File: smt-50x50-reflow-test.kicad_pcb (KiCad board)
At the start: 4 copper layers, 50 x 50 mm, 96 parts, among them J1 Conn_01x04_Pin, J2 Conn_01x02, J4 USB_C_Receptacle_USB2.0_14P, J8 Conn_01x04_Pin, J9 Conn_01x03_Pin, SW1 SW_Push, SW2 SW_Push, U1 ESP32-C6, U14 TMP117AIDRV, U15 BMP581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

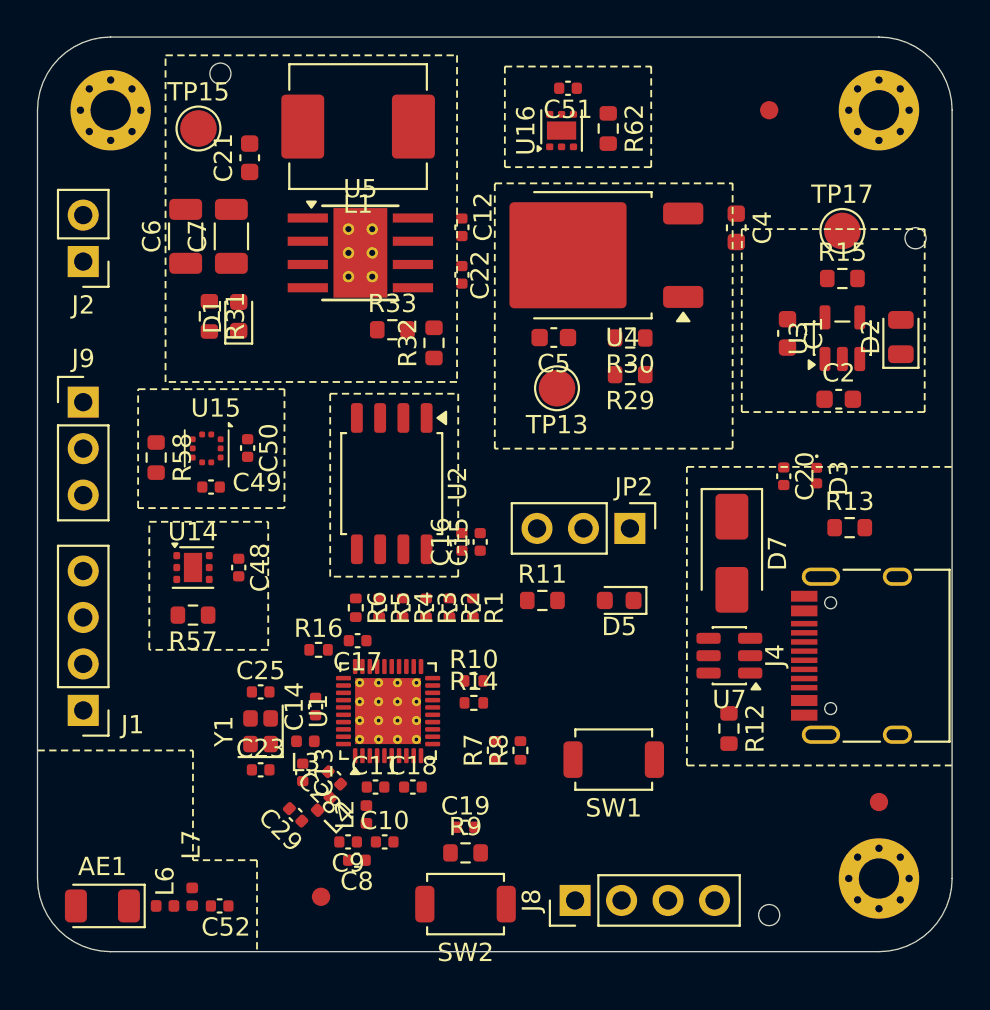
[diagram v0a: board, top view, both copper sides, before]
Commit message: pcb: align headers on a 2.54mm grid
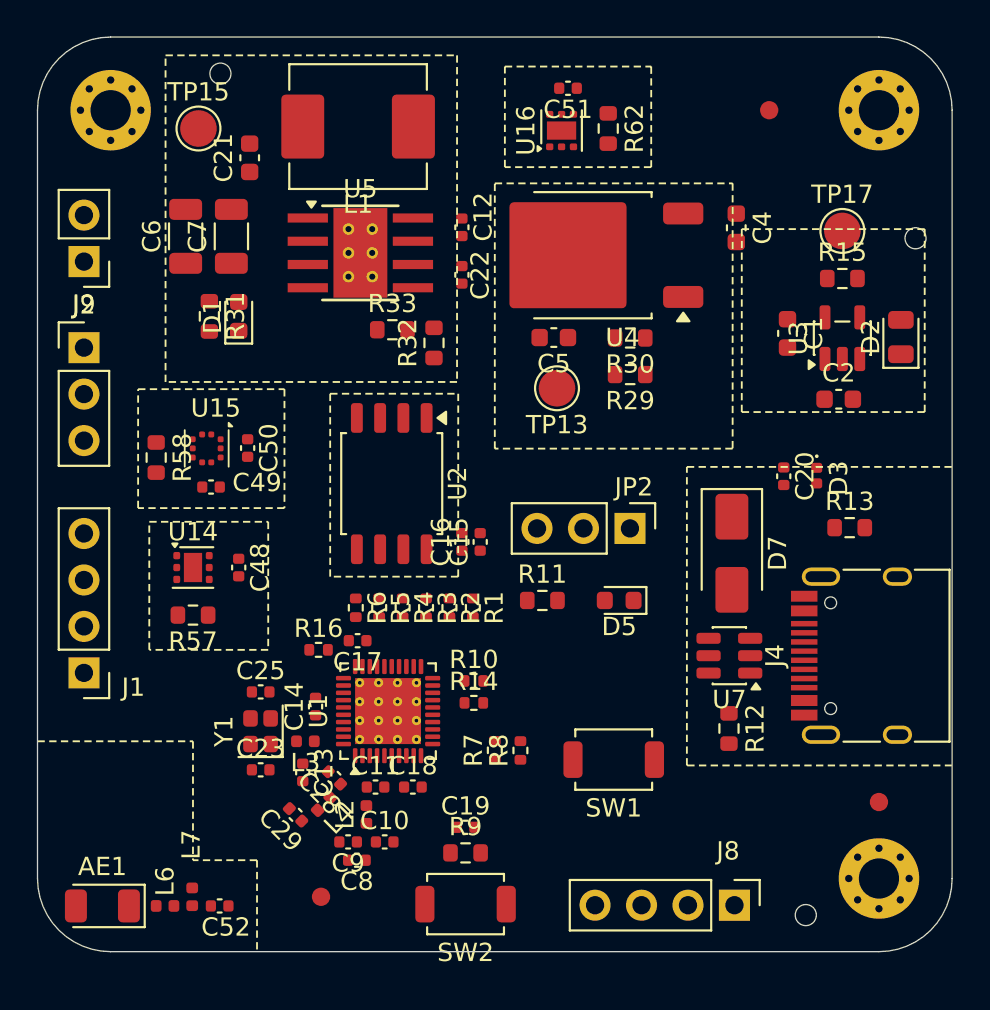
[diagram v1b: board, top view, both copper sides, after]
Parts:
- moved J8 8.71 mm to (173.1, 122.5), turned to -90 degrees
- moved J9 2.98 mm to (137.5, 92.0)
- moved J1 2.05 mm to (137.5, 109.8)
- moved REF** 2.00 mm to (177.0, 123.0)
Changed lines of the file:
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@@
 	(footprint "Connector_PinHeader_2.54mm:PinHeader_1x02_P2.54mm_Vertical"
 		(layer "F.Cu")
-		(at 137.5 87.275 180)
+		(at 137.54 87.275 180)
 		(descr "Through hole straight pin header, 1x02, 2.54mm pitch, single row")
 		(tags "Through hole pin header THT 1x02 2.54mm single row")
@@
 	(footprint "MountingHole:ToolingHole_1.152mm"
 		(layer "F.Cu")
-		(at 175 123)
+		(at 177 123)
 		(descr "Tooling Hole 1.152mm, 1.3mm solder mask, JLCPCB specification, https://jlcpcb.com/help/article/How-to-add-tooling-holes-for-PCB-assembly-order")
 		(tags "mounting")
@@
 			(polygon
 				(pts
-					(xy 175.7 123) (xy 175.679659 122.832479) (xy 175.619819 122.674694) (xy 175.523958 122.535814)
-					(xy 175.397645 122.423911) (xy 175.248223 122.345489) (xy 175.084376 122.305104) (xy 174.915624 122.305104)
-					(xy 174.751777 122.345489) (xy 174.602355 122.423911) (xy 174.476042 122.535814) (xy 174.380181 122.674694)
-					(xy 174.320341 122.832479) (xy 174.3 123) (xy 174.320341 123.167521) (xy 174.380181 123.325306)
-					(xy 174.476042 123.464186) (xy 174.602355 123.576089) (xy 174.751777 123.654511) (xy 174.915624 123.694896)
-					(xy 175.084376 123.694896) (xy 175.248223 123.654511) (xy 175.397645 123.576089) (xy 175.523958 123.464186)
-					(xy 175.619819 123.325306) (xy 175.679659 123.167521)
+					(xy 177.7 123) (xy 177.679659 122.832479) (xy 177.619819 122.674694) (xy 177.523958 122.535814)
+					(xy 177.397645 122.423911) (xy 177.248223 122.345489) (xy 177.084376 122.305104) (xy 176.915624 122.305104)
+					(xy 176.751777 122.345489) (xy 176.602355 122.423911) (xy 176.476042 122.535814) (xy 176.380181 122.674694)
+					(xy 176.320341 122.832479) (xy 176.3 123) (xy 176.320341 123.167521) (xy 176.380181 123.325306)
+					(xy 176.476042 123.464186) (xy 176.602355 123.576089) (xy 176.751777 123.654511) (xy 176.915624 123.694896)
+					(xy 177.084376 123.694896) (xy 177.248223 123.654511) (xy 177.397645 123.576089) (xy 177.523958 123.464186)
+					(xy 177.619819 123.325306) (xy 177.679659 123.167521)
 				)
 			)
@@
 	(footprint "Connector_PinHeader_2.54mm:PinHeader_1x04_P2.54mm_Vertical"
 		(layer "F.Cu")
-		(at 164.39 122.2 90)
+		(at 173.1 122.46 -90)
 		(descr "Through hole straight pin header, 1x04, 2.54mm pitch, single row")
 		(tags "Through hole pin header THT 1x04 2.54mm single row")
 		(property "Reference" "J8"
-			(at 0 -2.38 90)
+			(at -2.96 0.35 180)
 			(layer "F.SilkS")
 			(effects
@@
 		(attr through_hole exclude_from_bom)
 		(fp_line
-			(start -1.38 -1.38)
-			(end 0 -1.38)
+			(start -1.38 9)
+			(end 1.38 9)
 			(stroke
 				(width 0.12)
@@
 		)
 		(fp_line
-			(start -1.38 0)
-			(end -1.38 -1.38)
+			(start -1.38 1.27)
+			(end -1.38 9)
 			(stroke
 				(width 0.12)
@@
 		)
 		(fp_line
-			(start 1.38 1.27)
-			(end 1.38 9)
+			(start -1.38 1.27)
+			(end 1.38 1.27)
 			(stroke
 				(width 0.12)
@@
 		)
 		(fp_line
-			(start -1.38 1.27)
-			(end 1.38 1.27)
+			(start 1.38 1.27)
+			(end 1.38 9)
 			(stroke
 				(width 0.12)
@@
 		)
 		(fp_line
-			(start -1.38 1.27)
-			(end -1.38 9)
+			(start -1.38 0)
+			(end -1.38 -1.38)
 			(stroke
 				(width 0.12)
@@
 		)
 		(fp_line
-			(start -1.38 9)
-			(end 1.38 9)
+			(start -1.38 -1.38)
+			(end 0 -1.38)
 			(stroke
 				(width 0.12)
@@
 		)
 		(fp_line
-			(start 1.77 -1.77)
-			(end -1.77 -1.77)
+			(start -1.77 9.39)
+			(end 1.77 9.39)
 			(stroke
 				(width 0.05)
@@
 		)
 		(fp_line
-			(start -1.77 -1.77)
-			(end -1.77 9.39)
+			(start 1.77 9.39)
+			(end 1.77 -1.77)
 			(stroke
 				(width 0.05)
@@
 		)
 		(fp_line
-			(start 1.77 9.39)
-			(end 1.77 -1.77)
+			(start -1.77 -1.77)
+			(end -1.77 9.39)
 			(stroke
 				(width 0.05)
@@
 		)
 		(fp_line
-			(start -1.77 9.39)
-			(end 1.77 9.39)
+			(start 1.77 -1.77)
+			(end -1.77 -1.77)
 			(stroke
 				(width 0.05)
@@
 		)
 		(fp_line
-			(start 1.27 -1.27)
-			(end 1.27 8.89)
+			(start -1.27 8.89)
+			(end -1.27 -0.635)
 			(stroke
 				(width 0.1)
@@
 		)
 		(fp_line
-			(start -0.635 -1.27)
-			(end 1.27 -1.27)
+			(start 1.27 8.89)
+			(end -1.27 8.89)
 			(stroke
 				(width 0.1)
@@
 		)
 		(fp_line
-			(start 1.27 8.89)
-			(end -1.27 8.89)
+			(start -0.635 -1.27)
+			(end 1.27 -1.27)
 			(stroke
 				(width 0.1)
@@
 		)
 		(fp_line
-			(start -1.27 8.89)
-			(end -1.27 -0.635)
+			(start 1.27 -1.27)
+			(end 1.27 8.89)
 			(stroke
 				(width 0.1)
@@
 		)
 		(pad "1" thru_hole rect
-			(at 0 0 90)
+			(at 0 0 270)
 			(size 1.7 1.7)
 			(drill 1)
@@
 		)
 		(pad "2" thru_hole circle
-			(at 0 2.54 90)
+			(at 0 2.54 270)
 			(size 1.7 1.7)
 			(drill 1)
@@
 		)
 		(pad "3" thru_hole circle
-			(at 0 5.08 90)
+			(at 0 5.08 270)
 			(size 1.7 1.7)
 			(drill 1)
@@
 		)
 		(pad "4" thru_hole circle
-			(at 0 7.62 90)
+			(at 0 7.62 270)
 			(size 1.7 1.7)
 			(drill 1)
@@
 	(footprint "Connector_PinHeader_2.54mm:PinHeader_1x04_P2.54mm_Vertical"
 		(layer "F.Cu")
-		(at 137.5 111.81 180)
+		(at 137.54 109.76 180)
 		(descr "Through hole straight pin header, 1x04, 2.54mm pitch, single row")
 		(tags "Through hole pin header THT 1x04 2.54mm single row")
@@
 	(footprint "Connector_PinHeader_2.54mm:PinHeader_1x03_P2.54mm_Vertical"
 		(layer "F.Cu")
-		(at 137.5 94.96)
+		(at 137.54 91.98)
 		(descr "Through hole straight pin header, 1x03, 2.54mm pitch, single row")
 		(tags "Through hole pin header THT 1x03 2.54mm single row")
@@
 	)
 	(gr_line
-		(start 135 114)
-		(end 143.5 114)
+		(start 135 113.5)
+		(end 143.5 113.5)
 		(stroke
 			(width 0.1)
@@
 	)
 	(gr_line
-		(start 143.5 114)
+		(start 143.5 113.5)
 		(end 143.5 120)
 		(stroke

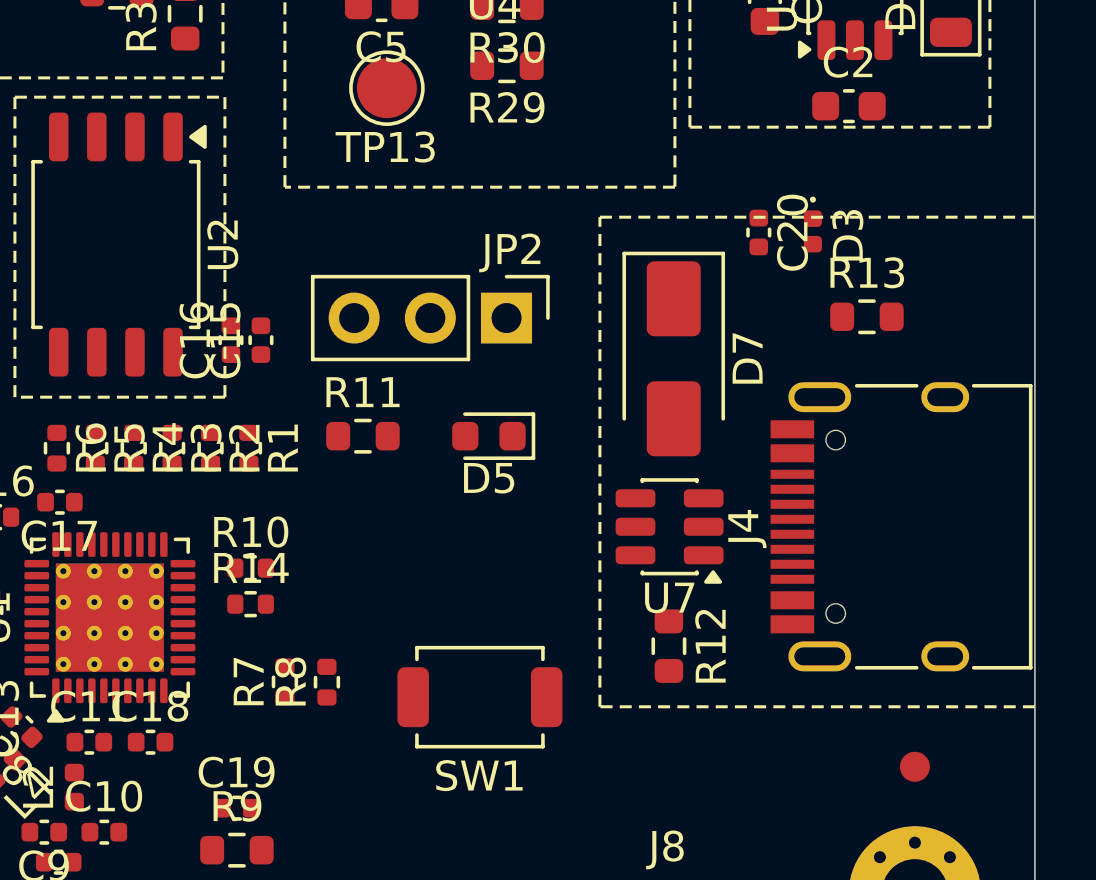
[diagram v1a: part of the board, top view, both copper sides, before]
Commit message: pcb: add usb routing
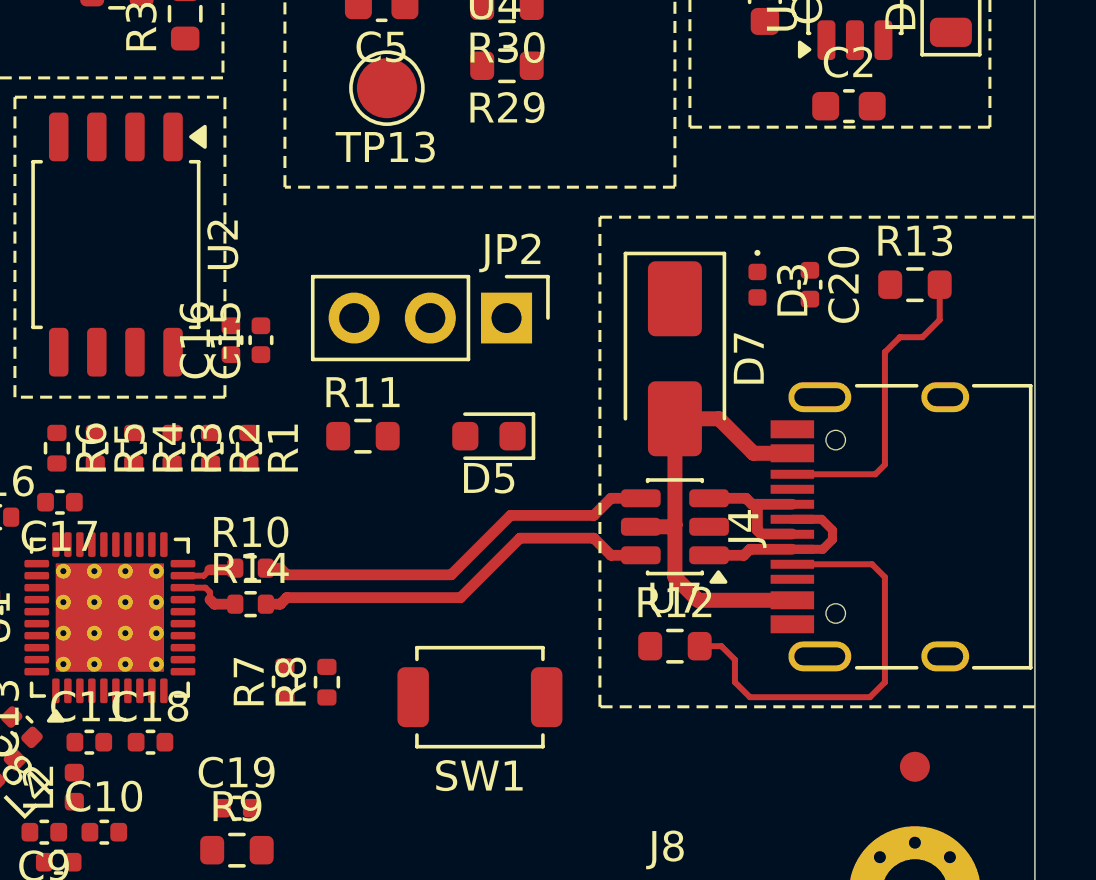
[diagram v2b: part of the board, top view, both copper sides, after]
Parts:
- moved D3 2.61 mm to (175.8, 100.8)
- moved C20 2.44 mm to (177.5, 100.8)
- moved R13 1.92 mm to (181.0, 100.8)
- moved R12 0.20 mm to (173.0, 112.8), turned to 0 degrees
- moved U7 0.18 mm to (173.0, 108.8)
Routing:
- net VBUS: track 0.00 -> 15.1 mm
- net Net-(J4-CC1): track 0.00 -> 14.3 mm
- net /D+: track 0.00 -> 13.6 mm
- net /D-: track 0.00 -> 13.6 mm
- net Net-(J4-CC2): track 0.00 -> 10.4 mm
- net Net-(J4-D--PadA7): track 0.00 -> 6.13 mm
- net Net-(J4-D+-PadA6): track 0.00 -> 4.95 mm
- net /ESP_D-: track 0.00 -> 2.12 mm
- net /ESP_D+: track 0.00 -> 1.85 mm

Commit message: pcb: add internal gnd planes
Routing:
- added copper zone on In1.Cu, net GND
- added copper zone on In2.Cu, net GND

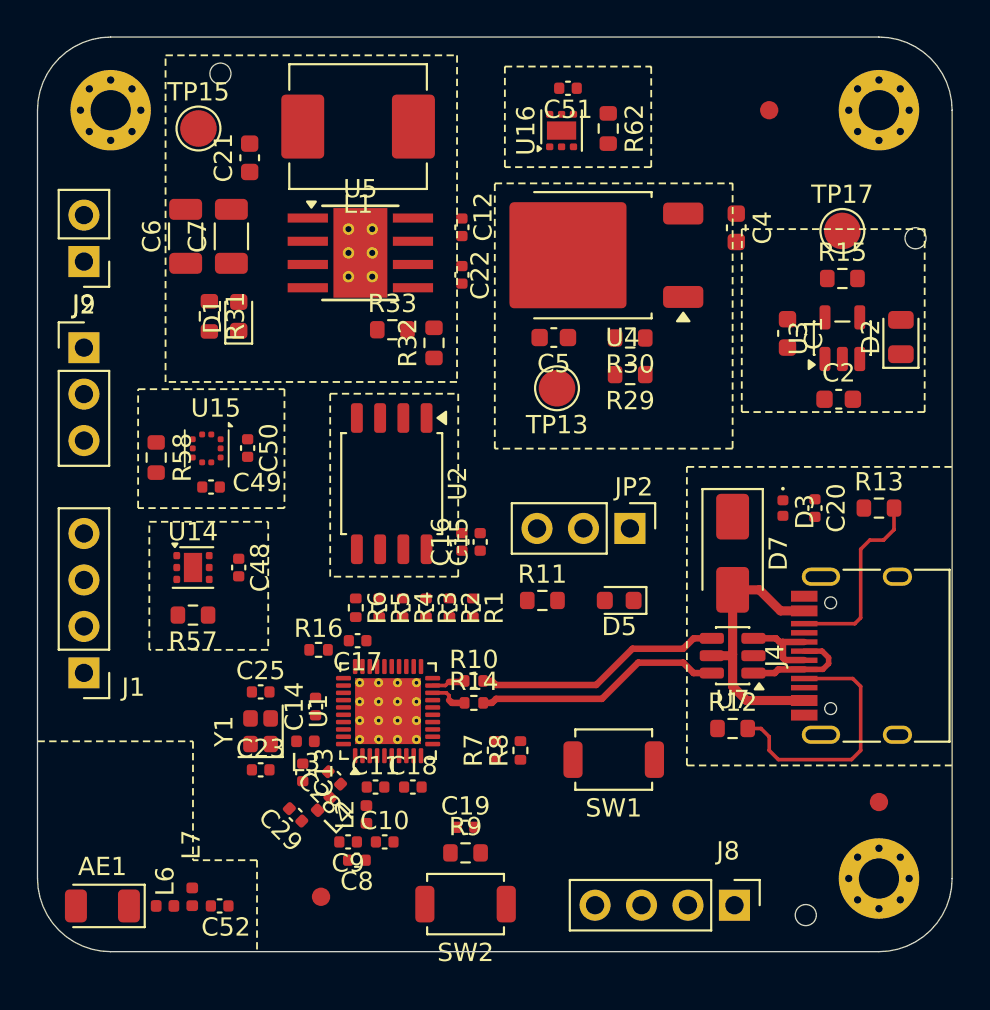
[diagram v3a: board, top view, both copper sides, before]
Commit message: pcb: add stiching vias
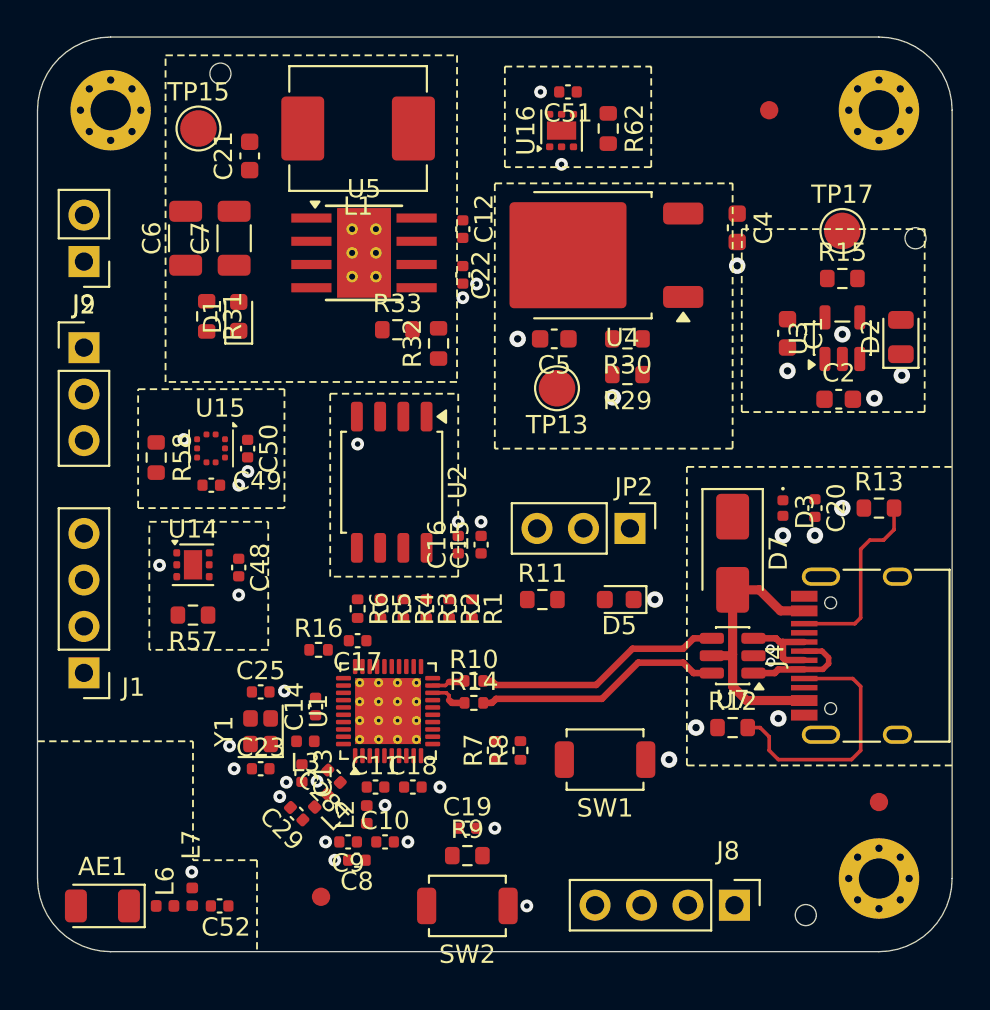
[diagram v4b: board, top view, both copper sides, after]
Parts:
- moved SW1 0.47 mm to (166.0, 114.5)
- moved R33 0.28 mm to (154.7, 91.0)
- moved R32 0.25 mm to (156.9, 91.8)
- moved C16 0.25 mm to (158.0, 102.8)
- moved U15 0.24 mm to (144.5, 97.5)
- moved L4 0.24 mm to (150.5, 116.8)
- moved C51 0.20 mm to (164.0, 78.0)
- moved U5 0.20 mm to (152.8, 86.8)
- moved C7 0.18 mm to (145.8, 86.0)
- moved R9 0.18 mm to (158.5, 119.8)
- moved C15 0.16 mm to (159.2, 102.8)
- moved R30 0.16 mm to (167.2, 91.5)
- moved R29 0.15 mm to (167.2, 93.5)
- moved U14 0.15 mm to (143.5, 103.8)
- moved R31 0.15 mm to (144.2, 90.3)
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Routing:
- net GND: vias 0 -> 42

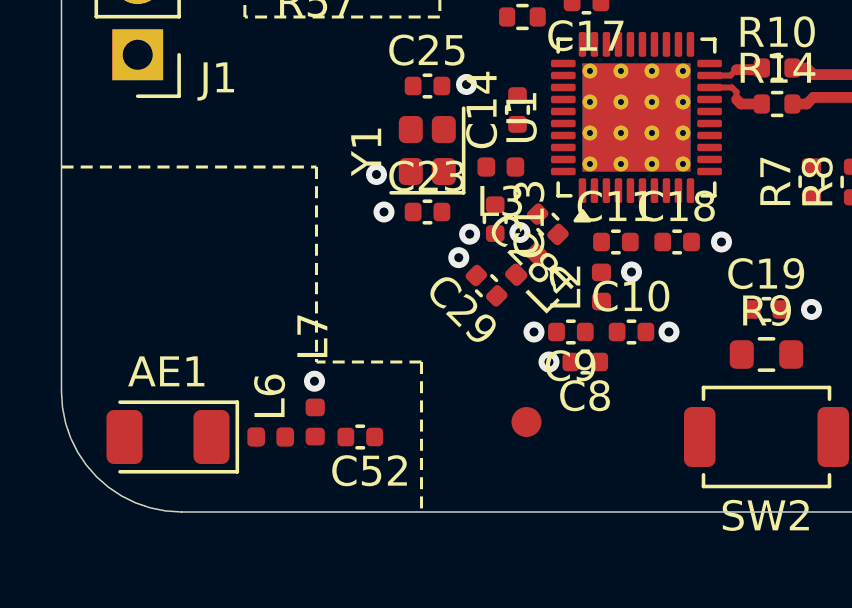
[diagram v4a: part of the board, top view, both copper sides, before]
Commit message: pcb: add rf routing
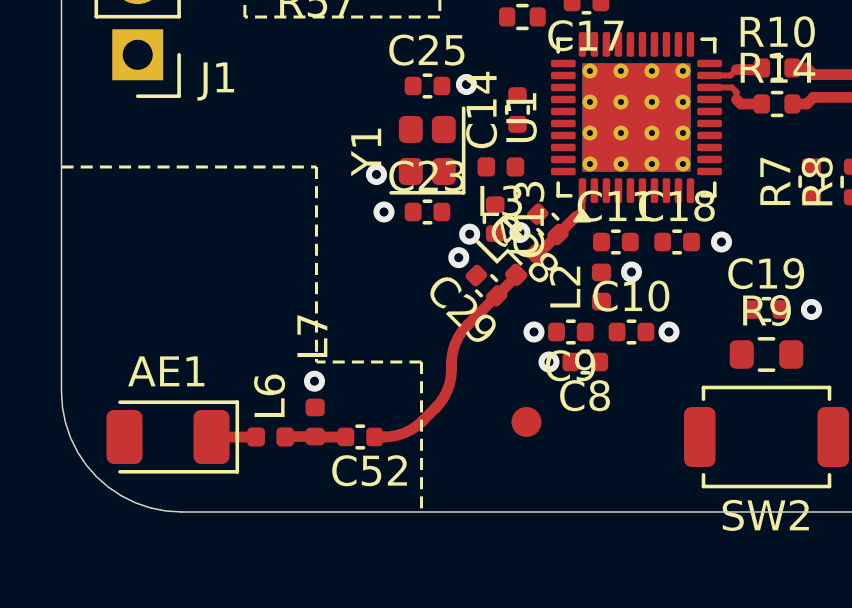
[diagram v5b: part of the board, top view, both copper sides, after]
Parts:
- turned L4 to 45 degrees
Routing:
- net /RF_TRANS: track 0.00 -> 7.73 mm
- net /RF_ESP: track 0.00 -> 2.78 mm
- net Net-(C52-Pad2): track 0.00 -> 2.03 mm
- net /RF_ANT: track 0.00 -> 1.49 mm
